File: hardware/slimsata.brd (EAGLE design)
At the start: 100 x 80 mm, 2 parts

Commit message: Stecker neu platziert
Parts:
- moved CON1 72.8 mm to (17.0, 58.9), turned to 90 degrees
- moved CON2 22.6 mm to (0.00, 21.1), turned to 270 degrees
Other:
- board size 100 x 80 mm -> 16.9 x 80 mm
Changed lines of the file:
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@@
 <board>
 <plain>
-<wire x1="0" y1="0" x2="100" y2="0" width="0" layer="20"/>
-<wire x1="100" y1="0" x2="100" y2="80" width="0" layer="20"/>
-<wire x1="100" y1="80" x2="0" y2="80" width="0" layer="20"/>
+<wire x1="0" y1="0" x2="16.942" y2="0" width="0" layer="20"/>
+<wire x1="16.942" y1="0" x2="16.942" y2="80" width="0" layer="20"/>
+<wire x1="16.942" y1="80" x2="0" y2="80" width="0" layer="20"/>
 <wire x1="0" y1="80" x2="0" y2="0" width="0" layer="20"/>
 </plain>
@@
 </autorouter>
 <elements>
-<element name="CON1" library="sata" package="MOLEX_47018" value="" x="59.69" y="0"/>
-<element name="CON2" library="sata" package="MOLEX_47300-1005" value="" x="19.05" y="8.89" rot="R180"/>
+<element name="CON1" library="sata" package="MOLEX_47018" value="" x="17.018" y="58.928" rot="R90"/>
+<element name="CON2" library="sata" package="MOLEX_47300-1005" value="" x="0" y="21.082" rot="R270"/>
 </elements>
 <signals>
@@
 <contactref element="CON2" pad="P6"/>
 <contactref element="CON2" pad="P5"/>
-<wire x1="35.4" y1="5.89" x2="40.98" y2="2.84" width="0" layer="19" extent="1-1"/>
-<wire x1="28.5" y1="2.44" x2="35.4" y2="5.89" width="0" layer="19" extent="1-1"/>
-<wire x1="27.5" y1="2.44" x2="28.5" y2="2.44" width="0" layer="19" extent="1-1"/>
-<wire x1="20.43" y1="2.29" x2="27.5" y2="2.44" width="0" layer="19" extent="1-1"/>
-<wire x1="62.865" y1="5.08" x2="20.43" y2="2.29" width="0" layer="19" extent="1-1"/>
-<wire x1="64.135" y1="5.08" x2="62.865" y2="5.08" width="0" layer="19" extent="1-1"/>
-<wire x1="61.595" y1="4.58" x2="62.865" y2="5.08" width="0" layer="19" extent="1-1"/>
-<wire x1="69.215" y1="5.08" x2="64.135" y2="5.08" width="0" layer="19" extent="1-1"/>
-<wire x1="71.755" y1="4.58" x2="69.215" y2="5.08" width="0" layer="19" extent="1-1"/>
-<wire x1="78.4" y1="2.84" x2="71.755" y2="4.58" width="0" layer="19" extent="1-1"/>
-<wire x1="2.7" y1="5.89" x2="78.4" y2="2.84" width="0" layer="19" extent="1-1"/>
+<wire x1="12.438" y1="70.993" x2="14.178" y2="77.638" width="0" layer="19" extent="1-1"/>
+<wire x1="11.938" y1="68.453" x2="12.438" y2="70.993" width="0" layer="19" extent="1-1"/>
+<wire x1="11.938" y1="63.373" x2="11.938" y2="68.453" width="0" layer="19" extent="1-1"/>
+<wire x1="11.938" y1="62.103" x2="11.938" y2="63.373" width="0" layer="19" extent="1-1"/>
+<wire x1="12.438" y1="60.833" x2="11.938" y2="62.103" width="0" layer="19" extent="1-1"/>
+<wire x1="14.178" y1="40.218" x2="12.438" y2="60.833" width="0" layer="19" extent="1-1"/>
+<wire x1="3" y1="37.432" x2="14.178" y2="40.218" width="0" layer="19" extent="1-1"/>
+<wire x1="6.45" y1="30.532" x2="3" y2="37.432" width="0" layer="19" extent="1-1"/>
+<wire x1="6.45" y1="29.532" x2="6.45" y2="30.532" width="0" layer="19" extent="1-1"/>
+<wire x1="6.6" y1="22.462" x2="6.45" y2="29.532" width="0" layer="19" extent="1-1"/>
+<wire x1="3" y1="4.732" x2="6.6" y2="22.462" width="0" layer="19" extent="1-1"/>
 </signal>
 <signal name="N$2">
@@
 <contactref element="CON1" pad="S7"/>
 <contactref element="CON2" pad="S7"/>
-<wire x1="47.625" y1="5.08" x2="43.815" y2="5.08" width="0" layer="19" extent="1-1"/>
-<wire x1="51.435" y1="5.08" x2="47.625" y2="5.08" width="0" layer="19" extent="1-1"/>
-<wire x1="17.29" y1="2.44" x2="51.435" y2="5.08" width="0" layer="19" extent="1-1"/>
-<wire x1="13.48" y1="2.44" x2="17.29" y2="2.44" width="0" layer="19" extent="1-1"/>
-<wire x1="9.67" y1="2.44" x2="13.48" y2="2.44" width="0" layer="19" extent="1-1"/>
+<wire x1="11.938" y1="46.863" x2="11.938" y2="50.673" width="0" layer="19" extent="1-1"/>
+<wire x1="11.938" y1="43.053" x2="11.938" y2="46.863" width="0" layer="19" extent="1-1"/>
+<wire x1="6.45" y1="19.322" x2="11.938" y2="43.053" width="0" layer="19" extent="1-1"/>
+<wire x1="6.45" y1="15.512" x2="6.45" y2="19.322" width="0" layer="19" extent="1-1"/>
+<wire x1="6.45" y1="11.702" x2="6.45" y2="15.512" width="0" layer="19" extent="1-1"/>
 </signal>
 <signal name="N$5">
 <contactref element="CON1" pad="S2"/>
 <contactref element="CON2" pad="S2"/>
-<wire x1="10.94" y1="2.44" x2="45.085" y2="5.08" width="0" layer="19" extent="1-1"/>
+<wire x1="6.45" y1="12.972" x2="11.938" y2="44.323" width="0" layer="19" extent="1-1"/>
 </signal>
 <signal name="N$6">
 <contactref element="CON1" pad="S3"/>
 <contactref element="CON2" pad="S3"/>
-<wire x1="12.21" y1="2.44" x2="46.355" y2="5.08" width="0" layer="19" extent="1-1"/>
+<wire x1="6.45" y1="14.242" x2="11.938" y2="45.593" width="0" layer="19" extent="1-1"/>
 </signal>
 <signal name="N$7">
 <contactref element="CON1" pad="S5"/>
 <contactref element="CON2" pad="S5"/>
-<wire x1="14.75" y1="2.44" x2="48.895" y2="5.08" width="0" layer="19" extent="1-1"/>
+<wire x1="6.45" y1="16.782" x2="11.938" y2="48.133" width="0" layer="19" extent="1-1"/>
 </signal>
 <signal name="N$8">
 <contactref element="CON1" pad="S6"/>
 <contactref element="CON2" pad="S6"/>
-<wire x1="16.02" y1="2.44" x2="50.165" y2="5.08" width="0" layer="19" extent="1-1"/>
+<wire x1="6.45" y1="18.052" x2="11.938" y2="49.403" width="0" layer="19" extent="1-1"/>
 </signal>
 <signal name="N$3">
@@
 <contactref element="CON2" pad="P2"/>
 <contactref element="CON2" pad="P3"/>
-<wire x1="66.675" y1="5.08" x2="65.405" y2="5.08" width="0" layer="19" extent="1-1"/>
-<wire x1="67.945" y1="5.08" x2="66.675" y2="5.08" width="0" layer="19" extent="1-1"/>
-<wire x1="24.5" y1="2.44" x2="65.405" y2="5.08" width="0" layer="19" extent="1-1"/>
-<wire x1="25.5" y1="2.44" x2="24.5" y2="2.44" width="0" layer="19" extent="1-1"/>
+<wire x1="11.938" y1="65.913" x2="11.938" y2="67.183" width="0" layer="19" extent="1-1"/>
+<wire x1="11.938" y1="64.643" x2="11.938" y2="65.913" width="0" layer="19" extent="1-1"/>
+<wire x1="6.45" y1="27.532" x2="11.938" y2="64.643" width="0" layer="19" extent="1-1"/>
+<wire x1="6.45" y1="26.532" x2="6.45" y2="27.532" width="0" layer="19" extent="1-1"/>
 </signal>
 </signals>

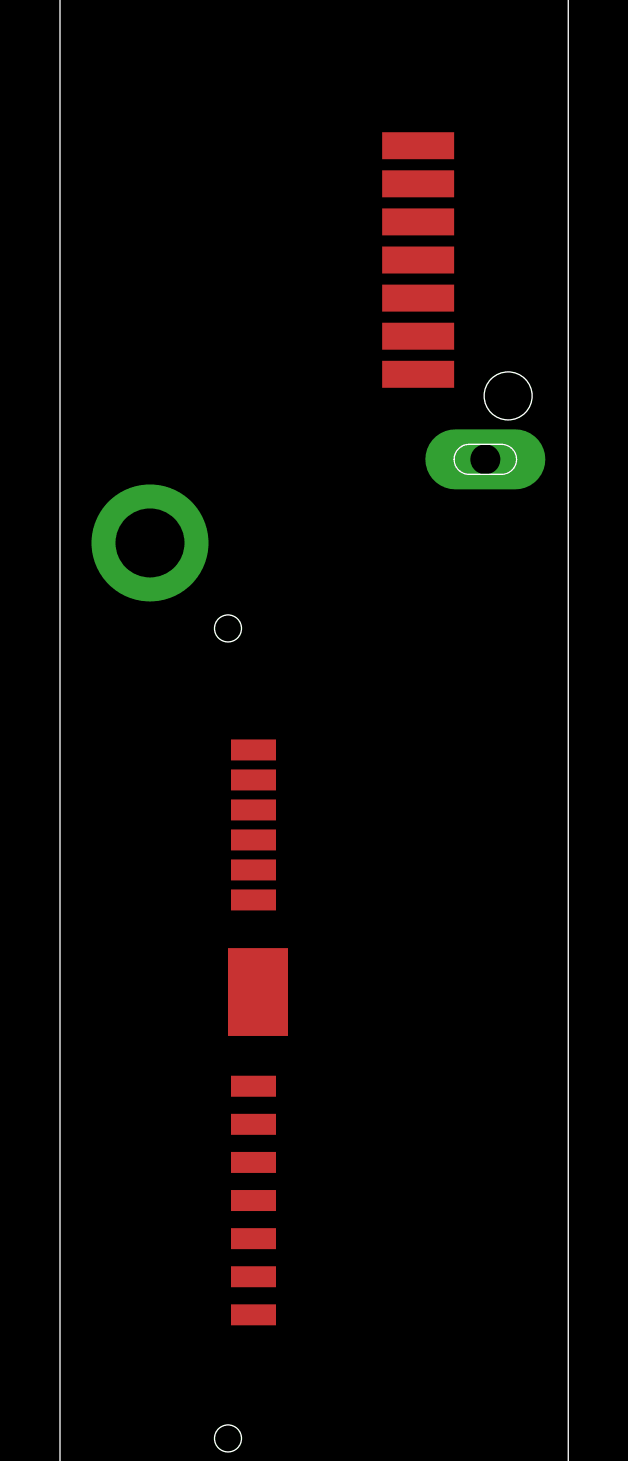
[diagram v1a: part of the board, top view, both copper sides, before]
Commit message: Signaleitungen geroutet
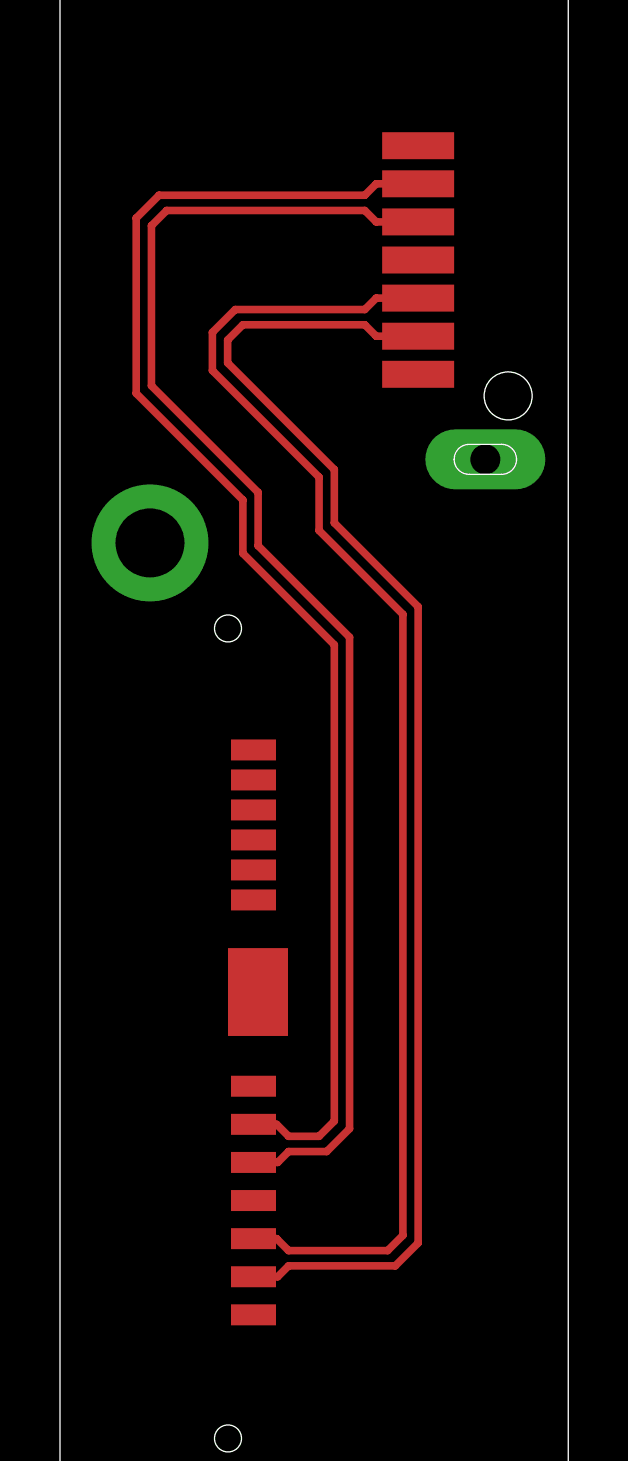
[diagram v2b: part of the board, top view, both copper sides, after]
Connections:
- removed net N$1: CON1.MECH1, CON1.MECH2, CON1.P10, CON1.P12, CON1.P4, CON1.P5, CON1.P6, CON2.MECH1, CON2.MECH2, CON2.MECH3, CON2.P5, CON2.P6
- removed net N$2: CON1.S1, CON1.S4, CON1.S7, CON2.S1, CON2.S4, CON2.S7
- new net GND: CON1.MECH1, CON1.MECH2, CON1.P10, CON1.P12, CON1.P4, CON1.P5, CON1.P6, CON1.S1, CON1.S4, CON1.S7, CON2.MECH1, CON2.MECH2, CON2.MECH3, CON2.P5, CON2.P6, CON2.S1, CON2.S4, CON2.S7
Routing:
- net N$8: track 0.00 -> 45.8 mm
- net N$7: track 0.00 -> 45.8 mm
- net N$6: track 0.00 -> 45.4 mm
- net N$5: track 0.00 -> 45.4 mm
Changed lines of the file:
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@@
 <setting verticaltext="up"/>
 </settings>
-<grid distance="10" unitdist="mil" unit="mil" style="dots" multiple="1" display="yes" altdistance="0.025" altunitdist="inch" altunit="inch"/>
+<grid distance="5" unitdist="mil" unit="mil" style="dots" multiple="1" display="yes" altdistance="0.025" altunitdist="inch" altunit="inch"/>
 <layers>
 <layer number="1" name="Top" color="4" fill="1" visible="yes" active="yes"/>
@@
 </elements>
 <signals>
-<signal name="N$1">
+<signal name="N$5">
+<contactref element="CON1" pad="S2"/>
+<contactref element="CON2" pad="S2"/>
+<wire x1="6.45" y1="12.972" x2="7.257" y2="12.972" width="0.254" layer="1"/>
+<wire x1="7.257" y1="12.972" x2="7.62" y2="13.335" width="0.254" layer="1"/>
+<wire x1="7.62" y1="13.335" x2="11.176" y2="13.335" width="0.254" layer="1"/>
+<wire x1="11.176" y1="13.335" x2="11.938" y2="14.097" width="0.254" layer="1"/>
+<wire x1="11.938" y1="14.097" x2="11.938" y2="35.306" width="0.254" layer="1"/>
+<wire x1="11.938" y1="35.306" x2="9.144" y2="38.1" width="0.254" layer="1"/>
+<wire x1="5.588" y1="44.196" x2="5.588" y2="43.434" width="0.254" layer="1"/>
+<wire x1="5.588" y1="43.434" x2="9.144" y2="39.878" width="0.254" layer="1"/>
+<wire x1="9.144" y1="39.878" x2="9.144" y2="38.1" width="0.254" layer="1"/>
+<wire x1="11.938" y1="44.323" x2="10.541" y2="44.323" width="0.254" layer="1"/>
+<wire x1="10.541" y1="44.323" x2="10.16" y2="44.704" width="0.254" layer="1"/>
+<wire x1="10.16" y1="44.704" x2="6.096" y2="44.704" width="0.254" layer="1"/>
+<wire x1="6.096" y1="44.704" x2="5.588" y2="44.196" width="0.254" layer="1"/>
+</signal>
+<signal name="N$6">
+<contactref element="CON1" pad="S3"/>
+<contactref element="CON2" pad="S3"/>
+<wire x1="6.45" y1="14.242" x2="7.221" y2="14.242" width="0.254" layer="1"/>
+<wire x1="7.221" y1="14.242" x2="7.62" y2="13.843" width="0.254" layer="1"/>
+<wire x1="7.62" y1="13.843" x2="10.922" y2="13.843" width="0.254" layer="1"/>
+<wire x1="10.922" y1="13.843" x2="11.43" y2="14.351" width="0.254" layer="1"/>
+<wire x1="11.43" y1="14.351" x2="11.43" y2="35.052" width="0.254" layer="1"/>
+<wire x1="11.43" y1="35.052" x2="8.636" y2="37.846" width="0.254" layer="1"/>
+<wire x1="5.08" y1="44.45" x2="5.08" y2="43.18" width="0.254" layer="1"/>
+<wire x1="5.08" y1="43.18" x2="8.636" y2="39.624" width="0.254" layer="1"/>
+<wire x1="8.636" y1="39.624" x2="8.636" y2="37.846" width="0.254" layer="1"/>
+<wire x1="11.938" y1="45.593" x2="10.541" y2="45.593" width="0.254" layer="1"/>
+<wire x1="10.541" y1="45.593" x2="10.16" y2="45.212" width="0.254" layer="1"/>
+<wire x1="10.16" y1="45.212" x2="5.842" y2="45.212" width="0.254" layer="1"/>
+<wire x1="5.842" y1="45.212" x2="5.08" y2="44.45" width="0.254" layer="1"/>
+</signal>
+<signal name="N$7">
+<contactref element="CON1" pad="S5"/>
+<contactref element="CON2" pad="S5"/>
+<wire x1="6.45" y1="16.782" x2="7.257" y2="16.782" width="0.254" layer="1"/>
+<wire x1="7.257" y1="16.782" x2="7.62" y2="17.145" width="0.254" layer="1"/>
+<wire x1="7.62" y1="17.145" x2="8.89" y2="17.145" width="0.254" layer="1"/>
+<wire x1="8.89" y1="17.145" x2="9.652" y2="17.907" width="0.254" layer="1"/>
+<wire x1="9.652" y1="17.907" x2="9.652" y2="34.29" width="0.254" layer="1"/>
+<wire x1="9.652" y1="34.29" x2="6.604" y2="37.338" width="0.254" layer="1"/>
+<wire x1="3.556" y1="48.514" x2="3.048" y2="48.006" width="0.254" layer="1"/>
+<wire x1="3.048" y1="48.006" x2="3.048" y2="42.672" width="0.254" layer="1"/>
+<wire x1="3.048" y1="42.672" x2="6.604" y2="39.116" width="0.254" layer="1"/>
+<wire x1="6.604" y1="39.116" x2="6.604" y2="37.338" width="0.254" layer="1"/>
+<wire x1="11.938" y1="48.133" x2="10.541" y2="48.133" width="0.254" layer="1"/>
+<wire x1="10.541" y1="48.133" x2="10.16" y2="48.514" width="0.254" layer="1"/>
+<wire x1="10.16" y1="48.514" x2="3.556" y2="48.514" width="0.254" layer="1"/>
+</signal>
+<signal name="N$8">
+<contactref element="CON1" pad="S6"/>
+<contactref element="CON2" pad="S6"/>
+<wire x1="6.45" y1="18.052" x2="7.221" y2="18.052" width="0.254" layer="1"/>
+<wire x1="7.221" y1="18.052" x2="7.62" y2="17.653" width="0.254" layer="1"/>
+<wire x1="7.62" y1="17.653" x2="8.636" y2="17.653" width="0.254" layer="1"/>
+<wire x1="8.636" y1="17.653" x2="9.144" y2="18.161" width="0.254" layer="1"/>
+<wire x1="9.144" y1="18.161" x2="9.144" y2="34.036" width="0.254" layer="1"/>
+<wire x1="9.144" y1="34.036" x2="6.096" y2="37.084" width="0.254" layer="1"/>
+<wire x1="3.302" y1="49.022" x2="2.54" y2="48.26" width="0.254" layer="1"/>
+<wire x1="2.54" y1="48.26" x2="2.54" y2="42.418" width="0.254" layer="1"/>
+<wire x1="2.54" y1="42.418" x2="6.096" y2="38.862" width="0.254" layer="1"/>
+<wire x1="6.096" y1="38.862" x2="6.096" y2="37.084" width="0.254" layer="1"/>
+<wire x1="11.938" y1="49.403" x2="10.541" y2="49.403" width="0.254" layer="1"/>
+<wire x1="10.541" y1="49.403" x2="10.16" y2="49.022" width="0.254" layer="1"/>
+<wire x1="10.16" y1="49.022" x2="3.302" y2="49.022" width="0.254" layer="1"/>
+</signal>
+<signal name="N$3">
+<contactref element="CON1" pad="P7"/>
+<contactref element="CON1" pad="P9"/>
+<contactref element="CON1" pad="P8"/>
+<contactref element="CON2" pad="P2"/>
+<contactref element="CON2" pad="P3"/>
+<wire x1="11.938" y1="65.913" x2="11.938" y2="67.183" width="0" layer="19" extent="1-1"/>
+<wire x1="11.938" y1="64.643" x2="11.938" y2="65.913" width="0" layer="19" extent="1-1"/>
+<wire x1="6.45" y1="27.532" x2="11.938" y2="64.643" width="0" layer="19" extent="1-1"/>
+<wire x1="6.45" y1="26.532" x2="6.45" y2="27.532" width="0" layer="19" extent="1-1"/>
+</signal>
+<signal name="GND">
+<contactref element="CON2" pad="S1"/>
+<contactref element="CON1" pad="S1"/>
+<contactref element="CON1" pad="S4"/>
+<contactref element="CON2" pad="S4"/>
+<contactref element="CON1" pad="S7"/>
+<contactref element="CON2" pad="S7"/>
 <contactref element="CON1" pad="MECH2"/>
 <contactref element="CON1" pad="MECH1"/>
@@
 <contactref element="CON2" pad="P5"/>
 <wire x1="12.438" y1="70.993" x2="14.178" y2="77.638" width="0" layer="19" extent="1-1"/>
-<wire x1="11.938" y1="68.453" x2="12.438" y2="70.993" width="0" layer="19" extent="1-1"/>
-<wire x1="11.938" y1="63.373" x2="11.938" y2="68.453" width="0" layer="19" extent="1-1"/>
-<wire x1="11.938" y1="62.103" x2="11.938" y2="63.373" width="0" layer="19" extent="1-1"/>
-<wire x1="12.438" y1="60.833" x2="11.938" y2="62.103" width="0" layer="19" extent="1-1"/>
-<wire x1="14.178" y1="40.218" x2="12.438" y2="60.833" width="0" layer="19" extent="1-1"/>
-<wire x1="3" y1="37.432" x2="14.178" y2="40.218" width="0" layer="19" extent="1-1"/>
-<wire x1="6.45" y1="30.532" x2="3" y2="37.432" width="0" layer="19" extent="1-1"/>
-<wire x1="6.45" y1="29.532" x2="6.45" y2="30.532" width="0" layer="19" extent="1-1"/>
-<wire x1="6.6" y1="22.462" x2="6.45" y2="29.532" width="0" layer="19" extent="1-1"/>
-<wire x1="3" y1="4.732" x2="6.6" y2="22.462" width="0" layer="19" extent="1-1"/>
-</signal>
-<signal name="N$2">
-<contactref element="CON2" pad="S1"/>
-<contactref element="CON1" pad="S1"/>
-<contactref element="CON1" pad="S4"/>
-<contactref element="CON2" pad="S4"/>
-<contactref element="CON1" pad="S7"/>
-<contactref element="CON2" pad="S7"/>
-<wire x1="11.938" y1="46.863" x2="11.938" y2="50.673" width="0" layer="19" extent="1-1"/>
-<wire x1="11.938" y1="43.053" x2="11.938" y2="46.863" width="0" layer="19" extent="1-1"/>
-<wire x1="6.45" y1="19.322" x2="11.938" y2="43.053" width="0" layer="19" extent="1-1"/>
-<wire x1="6.45" y1="15.512" x2="6.45" y2="19.322" width="0" layer="19" extent="1-1"/>
-<wire x1="6.45" y1="11.702" x2="6.45" y2="15.512" width="0" layer="19" extent="1-1"/>
-</signal>
-<signal name="N$5">
-<contactref element="CON1" pad="S2"/>
-<contactref element="CON2" pad="S2"/>
-<wire x1="6.45" y1="12.972" x2="11.938" y2="44.323" width="0" layer="19" extent="1-1"/>
-</signal>
-<signal name="N$6">
-<contactref element="CON1" pad="S3"/>
-<contactref element="CON2" pad="S3"/>
-<wire x1="6.45" y1="14.242" x2="11.938" y2="45.593" width="0" layer="19" extent="1-1"/>
-</signal>
-<signal name="N$7">
-<contactref element="CON1" pad="S5"/>
-<contactref element="CON2" pad="S5"/>
-<wire x1="6.45" y1="16.782" x2="11.938" y2="48.133" width="0" layer="19" extent="1-1"/>
-</signal>
-<signal name="N$8">
-<contactref element="CON1" pad="S6"/>
-<contactref element="CON2" pad="S6"/>
-<wire x1="6.45" y1="18.052" x2="11.938" y2="49.403" width="0" layer="19" extent="1-1"/>
-</signal>
-<signal name="N$3">
-<contactref element="CON1" pad="P7"/>
-<contactref element="CON1" pad="P9"/>
-<contactref element="CON1" pad="P8"/>
-<contactref element="CON2" pad="P2"/>
-<contactref element="CON2" pad="P3"/>
-<wire x1="11.938" y1="65.913" x2="11.938" y2="67.183" width="0" layer="19" extent="1-1"/>
-<wire x1="11.938" y1="64.643" x2="11.938" y2="65.913" width="0" layer="19" extent="1-1"/>
-<wire x1="6.45" y1="27.532" x2="11.938" y2="64.643" width="0" layer="19" extent="1-1"/>
-<wire x1="6.45" y1="26.532" x2="6.45" y2="27.532" width="0" layer="19" extent="1-1"/>
+<wire x1="14.178" y1="40.218" x2="11.938" y2="43.053" width="0" layer="19" extent="1-1"/>
 </signal>
 </signals>
